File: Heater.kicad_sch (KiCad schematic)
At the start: 11 parts, among them IC3 MCP1416T-E_OT, IC7 INA260AIPWR, J2 NTMFS5C612NLT1G, J4 Conn_01x02_Pin

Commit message: layout changes
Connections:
- net +3v3 is gone; now on net +5V: C19.1
- net HEATER_PWM renamed HEATER_PWN
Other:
- note removed: "^need to check this"
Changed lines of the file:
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@@
-		)
-	)
-	(text "^need to check this"
-		(exclude_from_sim no)
-		(at 66.04 32.766 0)
-		(effects
-			(font
-				(size 1.27 1.27)
-			)
 		)
 	)
@@
 		)
 	)
-	(hierarchical_label "HEATER_PWM"
-		(shape input)
-		(at 166.37 100.33 0)
-		(effects
-			(font
-				(size 1.27 1.27)
-			)
-			(justify left)
-		)
-	)
 	(hierarchical_label "SDA"
 		(shape input)
@@
 		(shape input)
 		(at 166.37 96.52 0)
+		(effects
+			(font
+				(size 1.27 1.27)
+			)
+			(justify left)
+		)
+	)
+	(hierarchical_label "HEATER_PWN"
+		(shape input)
+		(at 166.37 100.33 0)
 		(effects
 			(font
@@
 			)
 		)
-		(property "Value" "+3v3"
+		(property "Value" "+5V"
 			(at 86.36 24.13 0)
 			(effects

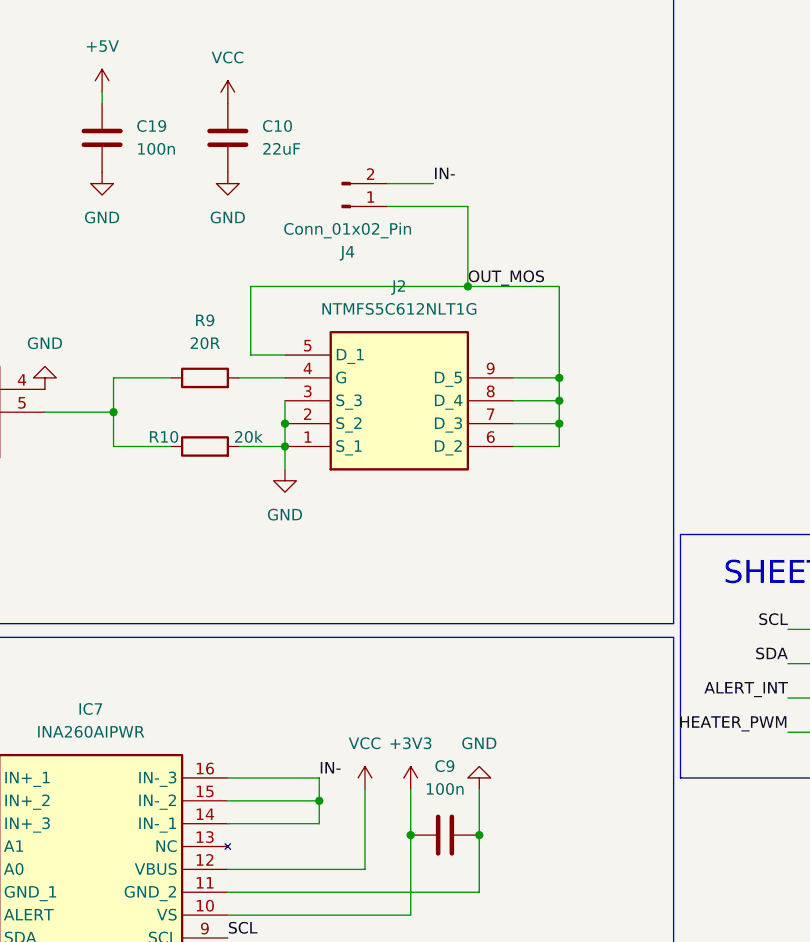
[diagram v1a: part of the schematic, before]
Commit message: Layout Changes, MPN Added
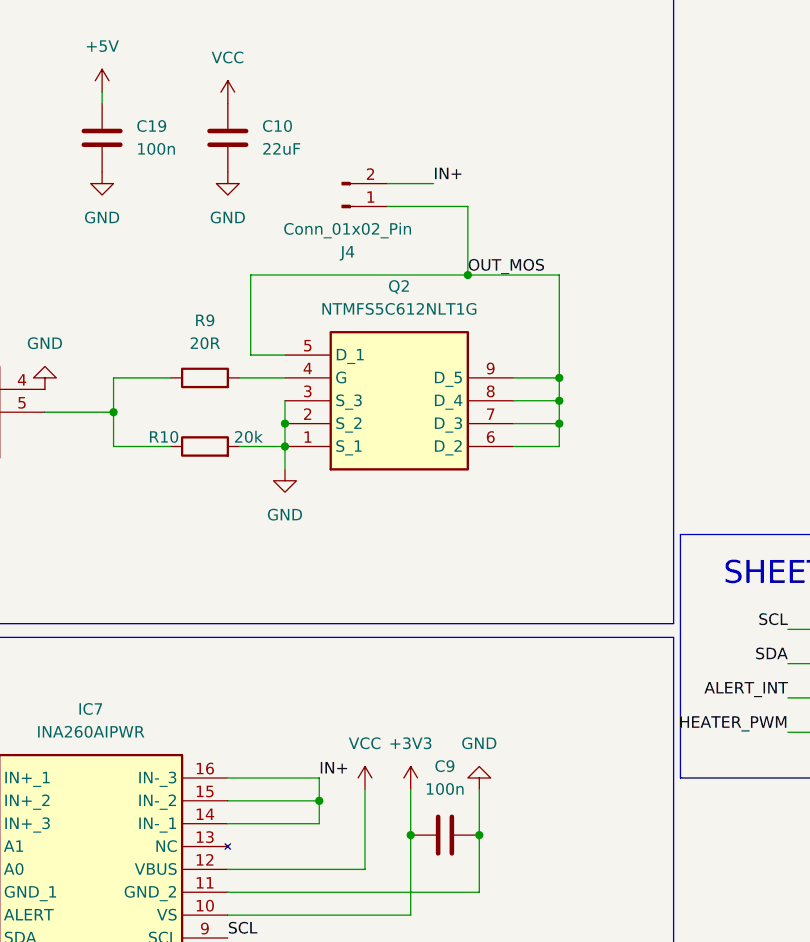
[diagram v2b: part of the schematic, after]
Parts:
- C19: MPN (none) -> GPC0402104-25
- IC3: MPN (none) -> MCP1416T-E/OT
- renumbered J2 to Q2
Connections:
- net IN- renamed IN+
